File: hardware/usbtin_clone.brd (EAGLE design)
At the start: 50 x 50 mm, 29 parts, among them IC1 18F14K50, IC3 MCP2551

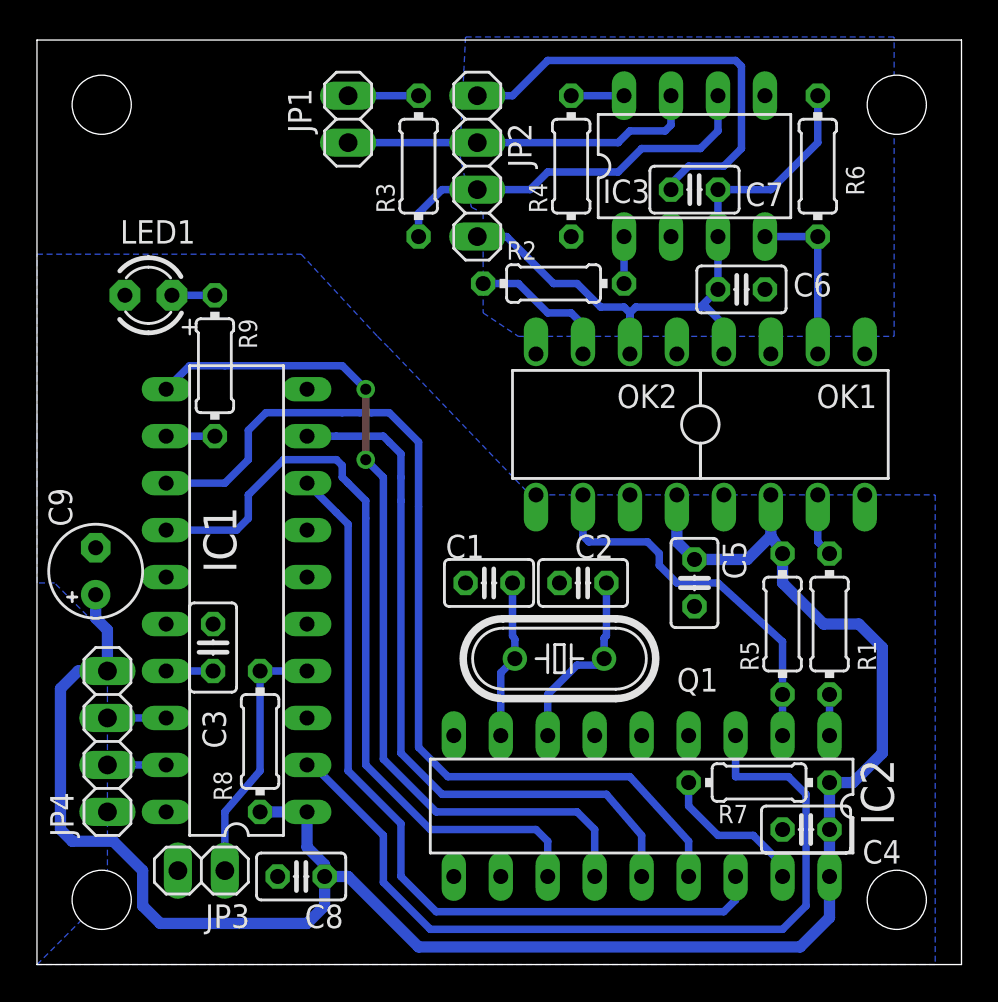
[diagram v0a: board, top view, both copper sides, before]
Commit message: add text on bottom layer to identify mirroring
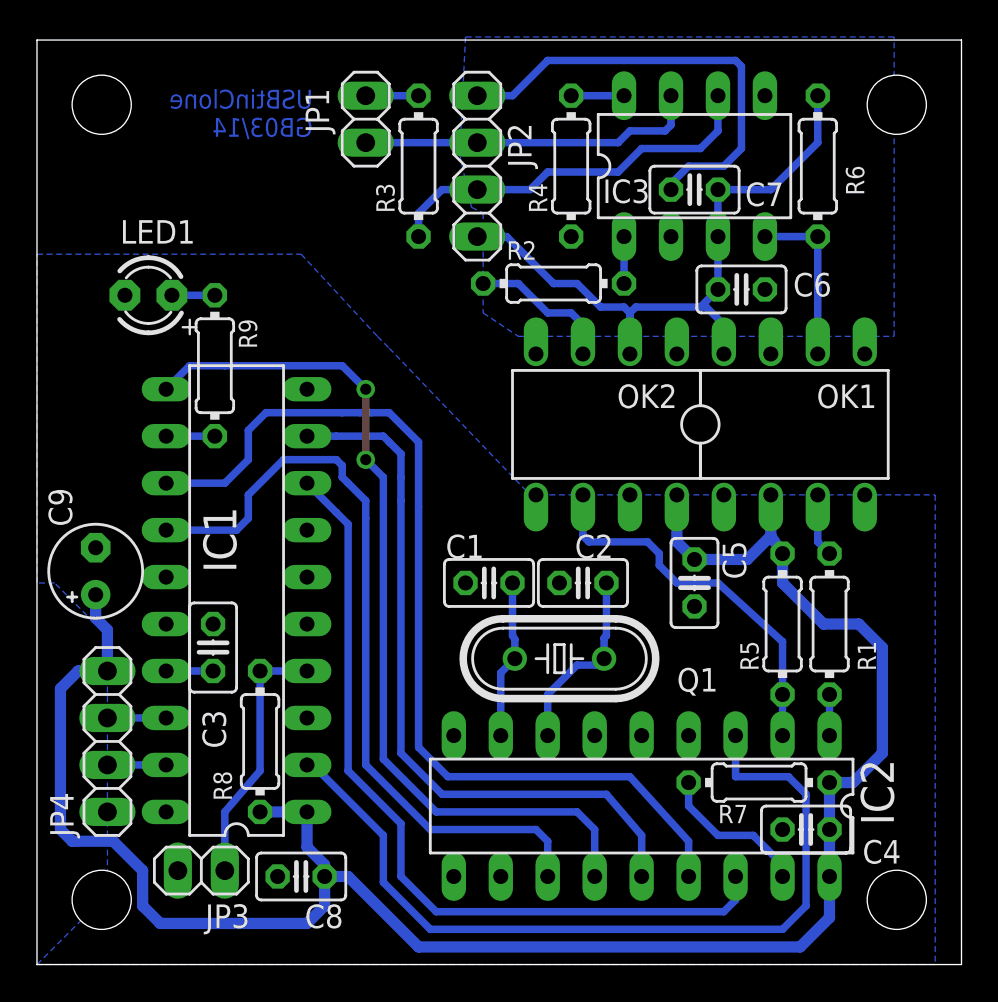
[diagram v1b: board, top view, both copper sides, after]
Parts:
- moved JP1 0.95 mm to (17.8, 45.7)
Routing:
- net N$11: track 19.4 -> 18.5 mm
- net N$10: track 3.81 -> 2.86 mm
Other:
- board text added: "USBtinClone GB03/14"
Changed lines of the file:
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@@
 <hole x="46.5" y="3.5" drill="3.2"/>
 <hole x="46.5" y="46.5" drill="3.2"/>
+<text x="14.9225" y="44.7675" size="1.016" layer="16" font="vector" rot="MR0">USBtinClone
+GB03/14</text>
 </plain>
 <attributes>
@@
 </element>
 <element name="R2" library="resistor" package="0204/7" value="" x="27.94" y="36.83"/>
-<element name="JP1" library="pinhead" package="1X02" value="" x="16.8275" y="45.72" smashed="yes" rot="R270">
-<attribute name="NAME" x="13.5763" y="47.3837" size="1.27" layer="25" ratio="10" rot="R270"/>
-<attribute name="VALUE" x="13.6525" y="48.26" size="1.27" layer="27" rot="R270"/>
+<element name="JP1" library="pinhead" package="1X02" value="" x="17.78" y="45.72" smashed="yes" rot="R270">
+<attribute name="NAME" x="14.5288" y="47.3837" size="1.27" layer="25" ratio="10" rot="R270"/>
+<attribute name="VALUE" x="14.605" y="48.26" size="1.27" layer="27" rot="R270"/>
 </element>
 <element name="R3" library="resistor" package="0204/7" value="" x="20.6375" y="43.18" rot="R90"/>
@@
 <contactref element="R1" pad="2"/>
 <contactref element="OK1" pad="3"/>
-<wire x1="42.8625" y1="22.225" x2="42.545" y2="22.5425" width="0.4064" layer="16"/>
-<wire x1="42.545" y1="22.5425" x2="42.2275" y2="22.86" width="0.4064" layer="16"/>
+<wire x1="42.8625" y1="22.225" x2="42.2275" y2="22.86" width="0.4064" layer="16"/>
 <wire x1="42.2275" y1="22.86" x2="42.2275" y2="25.4" width="0.4064" layer="16"/>
 </signal>
@@
 <contactref element="R3" pad="2"/>
 <contactref element="JP1" pad="1"/>
-<wire x1="16.8275" y1="46.99" x2="20.6375" y2="46.99" width="0.4064" layer="16"/>
+<wire x1="17.78" y1="46.99" x2="20.6375" y2="46.99" width="0.4064" layer="16"/>
 </signal>
 <signal name="N$11">
@@
 <wire x1="33.9725" y1="45.085" x2="34.29" y2="45.4025" width="0.4064" layer="16"/>
 <wire x1="34.29" y1="45.4025" x2="34.29" y2="46.99" width="0.4064" layer="16"/>
-<wire x1="16.8275" y1="44.45" x2="23.8125" y2="44.45" width="0.4064" layer="16"/>
+<wire x1="17.78" y1="44.45" x2="23.8125" y2="44.45" width="0.4064" layer="16"/>
 </signal>
 <signal name="N$12">
@@
 </board>
 </drawing>
+<compatibility>
+<note version="6.3" minversion="6.2.2" severity="warning">
+Since Version 6.2.2 text objects can contain more than one line,
+which will not be processed correctly with this version.
+</note>
+</compatibility>
 </eagle>

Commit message: minor BRD changes
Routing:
- net N$15: track 45.1 -> 44.4 mm
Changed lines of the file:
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@@
 <wire x1="42.8625" y1="4.7625" x2="42.8625" y2="7.3025" width="0.6096" layer="16"/>
 <wire x1="42.8625" y1="7.3025" x2="42.8625" y2="9.8425" width="0.6096" layer="16"/>
-<wire x1="40.3225" y1="22.225" x2="39.6875" y2="23.1775" width="0.6096" layer="16"/>
-<wire x1="39.6875" y1="23.1775" x2="39.6875" y2="25.4" width="0.6096" layer="16"/>
+<wire x1="39.6875" y1="23.495" x2="39.6875" y2="25.4" width="0.6096" layer="16"/>
 <wire x1="15.5575" y1="4.7625" x2="16.8275" y2="4.7625" width="0.6096" layer="16"/>
 <wire x1="16.8275" y1="4.7625" x2="20.6375" y2="0.9525" width="0.6096" layer="16"/>
@@
 <wire x1="41.275" y1="0.9525" x2="42.8625" y2="2.54" width="0.6096" layer="16"/>
 <wire x1="42.8625" y1="2.54" x2="42.8625" y2="4.7625" width="0.6096" layer="16"/>
-<wire x1="35.56" y1="21.9075" x2="38.4175" y2="21.9075" width="0.6096" layer="16"/>
-<wire x1="38.4175" y1="21.9075" x2="39.6875" y2="23.1775" width="0.6096" layer="16"/>
+<wire x1="35.56" y1="21.9075" x2="38.1" y2="21.9075" width="0.6096" layer="16"/>
+<wire x1="38.1" y1="21.9075" x2="39.6875" y2="23.495" width="0.6096" layer="16"/>
 <wire x1="35.56" y1="21.9075" x2="34.6075" y2="22.86" width="0.6096" layer="16"/>
 <wire x1="34.6075" y1="22.86" x2="34.6075" y2="25.4" width="0.6096" layer="16"/>
@@
 <wire x1="2.2225" y1="15.875" x2="1.27" y2="14.9225" width="0.6096" layer="16"/>
 <wire x1="1.27" y1="14.9225" x2="1.27" y2="7.3025" width="0.6096" layer="16"/>
-<wire x1="1.27" y1="7.3025" x2="1.905" y2="6.6675" width="0.6096" layer="16"/>
-<wire x1="1.905" y1="6.6675" x2="4.1275" y2="6.6675" width="0.6096" layer="16"/>
-<wire x1="4.1275" y1="6.6675" x2="5.715" y2="5.08" width="0.6096" layer="16"/>
+<wire x1="1.27" y1="7.3025" x2="1.905" y2="6.35" width="0.6096" layer="16"/>
+<wire x1="1.905" y1="6.35" x2="4.445" y2="6.35" width="0.6096" layer="16"/>
+<wire x1="4.445" y1="6.35" x2="5.715" y2="5.08" width="0.6096" layer="16"/>
 <wire x1="5.715" y1="5.08" x2="5.715" y2="3.175" width="0.6096" layer="16"/>
 <wire x1="5.715" y1="3.175" x2="6.6675" y2="2.2225" width="0.6096" layer="16"/>
@@
 <wire x1="14.605" y1="2.2225" x2="15.5575" y2="3.175" width="0.6096" layer="16"/>
 <wire x1="15.5575" y1="3.175" x2="15.5575" y2="4.7625" width="0.6096" layer="16"/>
+<wire x1="39.6875" y1="23.495" x2="40.3225" y2="22.86" width="0.6096" layer="16"/>
+<wire x1="40.3225" y1="22.86" x2="40.3225" y2="22.225" width="0.6096" layer="16"/>
 </signal>
 <signal name="N$1">
@@
 <wire x1="21.2725" y1="1.905" x2="40.3225" y2="1.905" width="0.4064" layer="16"/>
 <wire x1="40.3225" y1="1.905" x2="41.5925" y2="3.175" width="0.4064" layer="16"/>
-<wire x1="41.5925" y1="3.175" x2="41.5925" y2="9.2075" width="0.4064" layer="16"/>
-<wire x1="41.5925" y1="9.2075" x2="40.64" y2="10.16" width="0.4064" layer="16"/>
-<wire x1="40.64" y1="10.16" x2="37.7825" y2="10.16" width="0.4064" layer="16"/>
-<wire x1="37.7825" y1="10.16" x2="37.7825" y2="12.3825" width="0.4064" layer="16"/>
+<wire x1="41.5925" y1="3.175" x2="41.5925" y2="8.5725" width="0.4064" layer="16"/>
+<wire x1="41.5925" y1="8.5725" x2="40.005" y2="10.16" width="0.4064" layer="16"/>
+<wire x1="40.005" y1="10.16" x2="38.4175" y2="10.16" width="0.4064" layer="16"/>
+<wire x1="38.4175" y1="10.16" x2="37.7825" y2="10.795" width="0.4064" layer="16"/>
+<wire x1="37.7825" y1="10.795" x2="37.7825" y2="12.3825" width="0.4064" layer="16"/>
 </signal>
 <signal name="N$16">
@@
 <wire x1="21.59" y1="8.255" x2="18.7325" y2="11.1125" width="0.4064" layer="16"/>
 <wire x1="18.7325" y1="11.1125" x2="18.7325" y2="26.3525" width="0.4064" layer="16"/>
-<wire x1="10.16" y1="32.385" x2="8.255" y2="32.385" width="0.4064" layer="16"/>
 <wire x1="8.255" y1="32.385" x2="6.985" y2="31.115" width="0.4064" layer="16"/>
-<wire x1="18.7325" y1="26.3525" x2="17.78" y2="27.305" width="0.4064" layer="16"/>
-<via x="17.78" y="27.305" extent="1-16" drill="0.6" shape="square"/>
-<wire x1="17.78" y1="27.305" x2="17.78" y2="31.115" width="0.4064" layer="1"/>
-<via x="17.78" y="31.115" extent="1-16" drill="0.6" shape="square"/>
-<wire x1="17.78" y1="31.115" x2="16.51" y2="32.385" width="0.4064" layer="16"/>
-<wire x1="16.51" y1="32.385" x2="10.16" y2="32.385" width="0.4064" layer="16"/>
+<wire x1="18.7325" y1="26.3525" x2="18.0975" y2="26.9875" width="0.4064" layer="16"/>
+<via x="18.0975" y="26.9875" extent="1-16" drill="0.6" shape="square"/>
+<wire x1="18.0975" y1="26.9875" x2="18.0975" y2="31.4325" width="0.4064" layer="1"/>
+<via x="18.0975" y="31.4325" extent="1-16" drill="0.6" shape="square"/>
+<wire x1="18.0975" y1="31.4325" x2="17.145" y2="32.385" width="0.4064" layer="16"/>
+<wire x1="17.145" y1="32.385" x2="8.255" y2="32.385" width="0.4064" layer="16"/>
 </signal>
 <signal name="N$26">

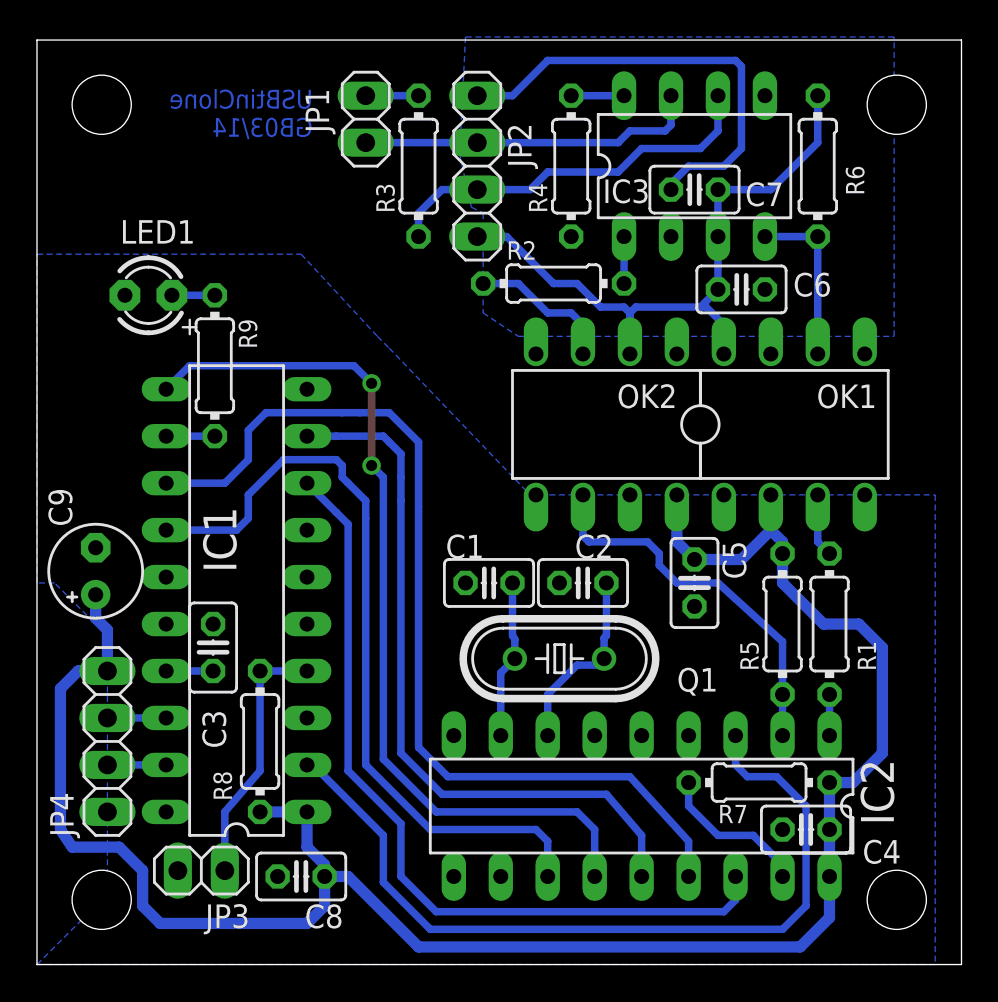
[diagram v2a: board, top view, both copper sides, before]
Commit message: add vallues to schematic
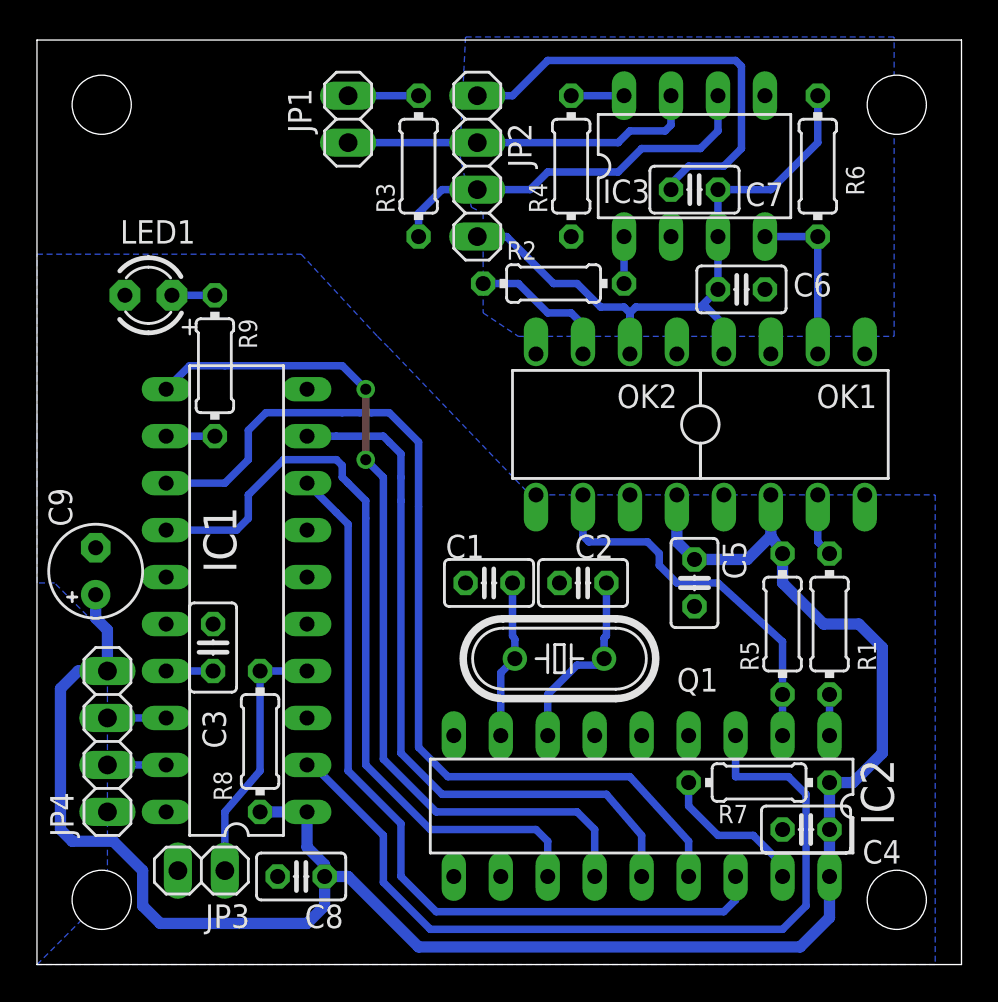
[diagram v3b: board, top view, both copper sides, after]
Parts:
- C1, C2: value (none) -> 22p
- C3, C4, C5, C6, C7, C8: value (none) -> 100n
- C9: value (none) -> 4,7u
- R1, R2, R5, R6, R9: value (none) -> 390
- R3: value (none) -> 120
- R4, R7, R8: value (none) -> 1k
- moved JP1 0.95 mm to (16.8, 45.7)
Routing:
- net N$11: track 18.5 -> 19.4 mm
- net N$10: track 2.86 -> 3.81 mm
- net N$15: track 44.4 -> 45.1 mm
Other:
- board text removed: "USBtinClone GB03/14"

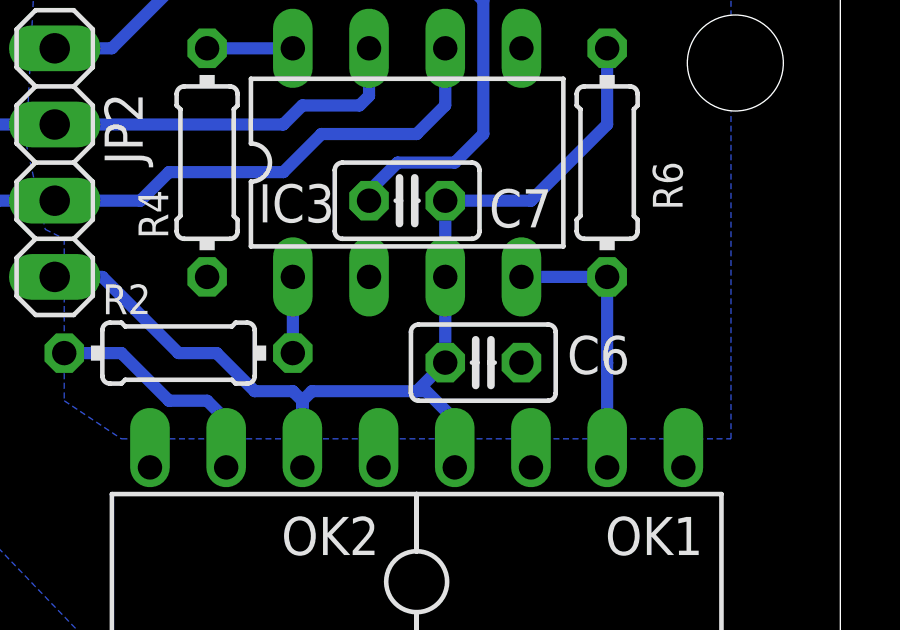
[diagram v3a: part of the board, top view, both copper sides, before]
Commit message: grr - CAN TX/RX fault
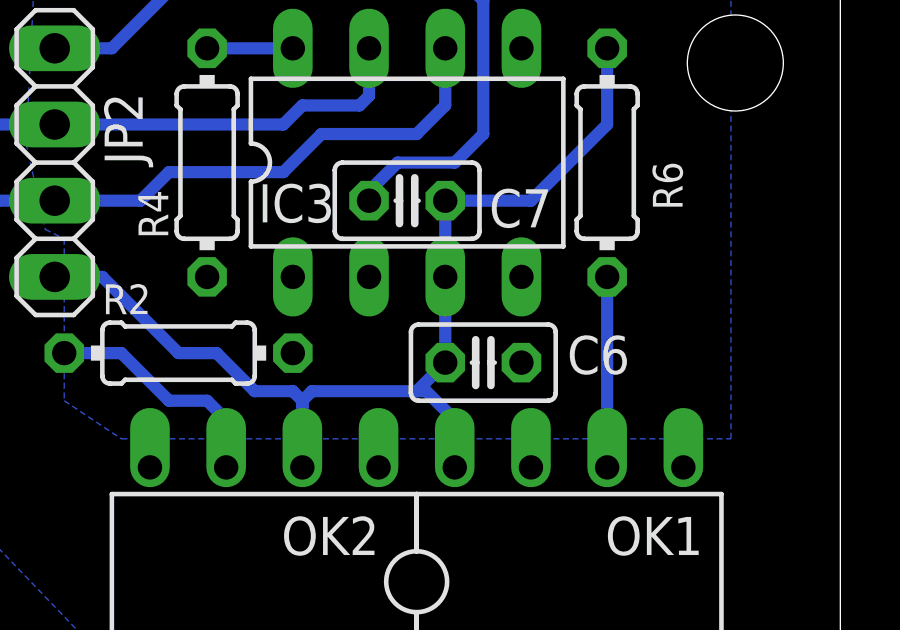
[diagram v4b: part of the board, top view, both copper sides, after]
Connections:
- net N$6: now also IC3.1; no longer IC3.4
- net N$8: now also IC3.4; no longer IC3.1
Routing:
- net N$6: track 9.21 -> 6.35 mm
- net N$8: track 2.54 -> 0.00 mm
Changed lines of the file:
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@@
 <signal name="N$6">
 <contactref element="OK1" pad="6"/>
-<contactref element="IC3" pad="4"/>
 <contactref element="R6" pad="1"/>
-<wire x1="39.37" y1="39.37" x2="42.2275" y2="39.37" width="0.4064" layer="16"/>
 <wire x1="42.2275" y1="39.37" x2="42.2275" y2="36.5125" width="0.4064" layer="16"/>
 <wire x1="42.2275" y1="36.5125" x2="42.2275" y2="36.195" width="0.4064" layer="16"/>
 <wire x1="42.2275" y1="36.195" x2="42.2275" y2="33.02" width="0.4064" layer="16"/>
-</signal>
-<signal name="N$8">
-<contactref element="R2" pad="2"/>
 <contactref element="IC3" pad="1"/>
-<wire x1="31.75" y1="36.83" x2="31.75" y2="39.37" width="0.4064" layer="16"/>
+<wire x1="31.75" y1="39.37" x2="42.2275" y2="39.37" width="0" layer="19" extent="1-1"/>
 </signal>
 <signal name="N$9">
@@
 <contactref element="IC2" pad="10"/>
 </signal>
+<signal name="N$8">
+<contactref element="IC3" pad="4"/>
+<contactref element="R2" pad="2"/>
+<wire x1="31.75" y1="36.83" x2="39.37" y2="39.37" width="0" layer="19" extent="1-1"/>
+</signal>
 </signals>
